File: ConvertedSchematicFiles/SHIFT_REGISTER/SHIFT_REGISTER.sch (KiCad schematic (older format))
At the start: 10 parts, among them U1 7494

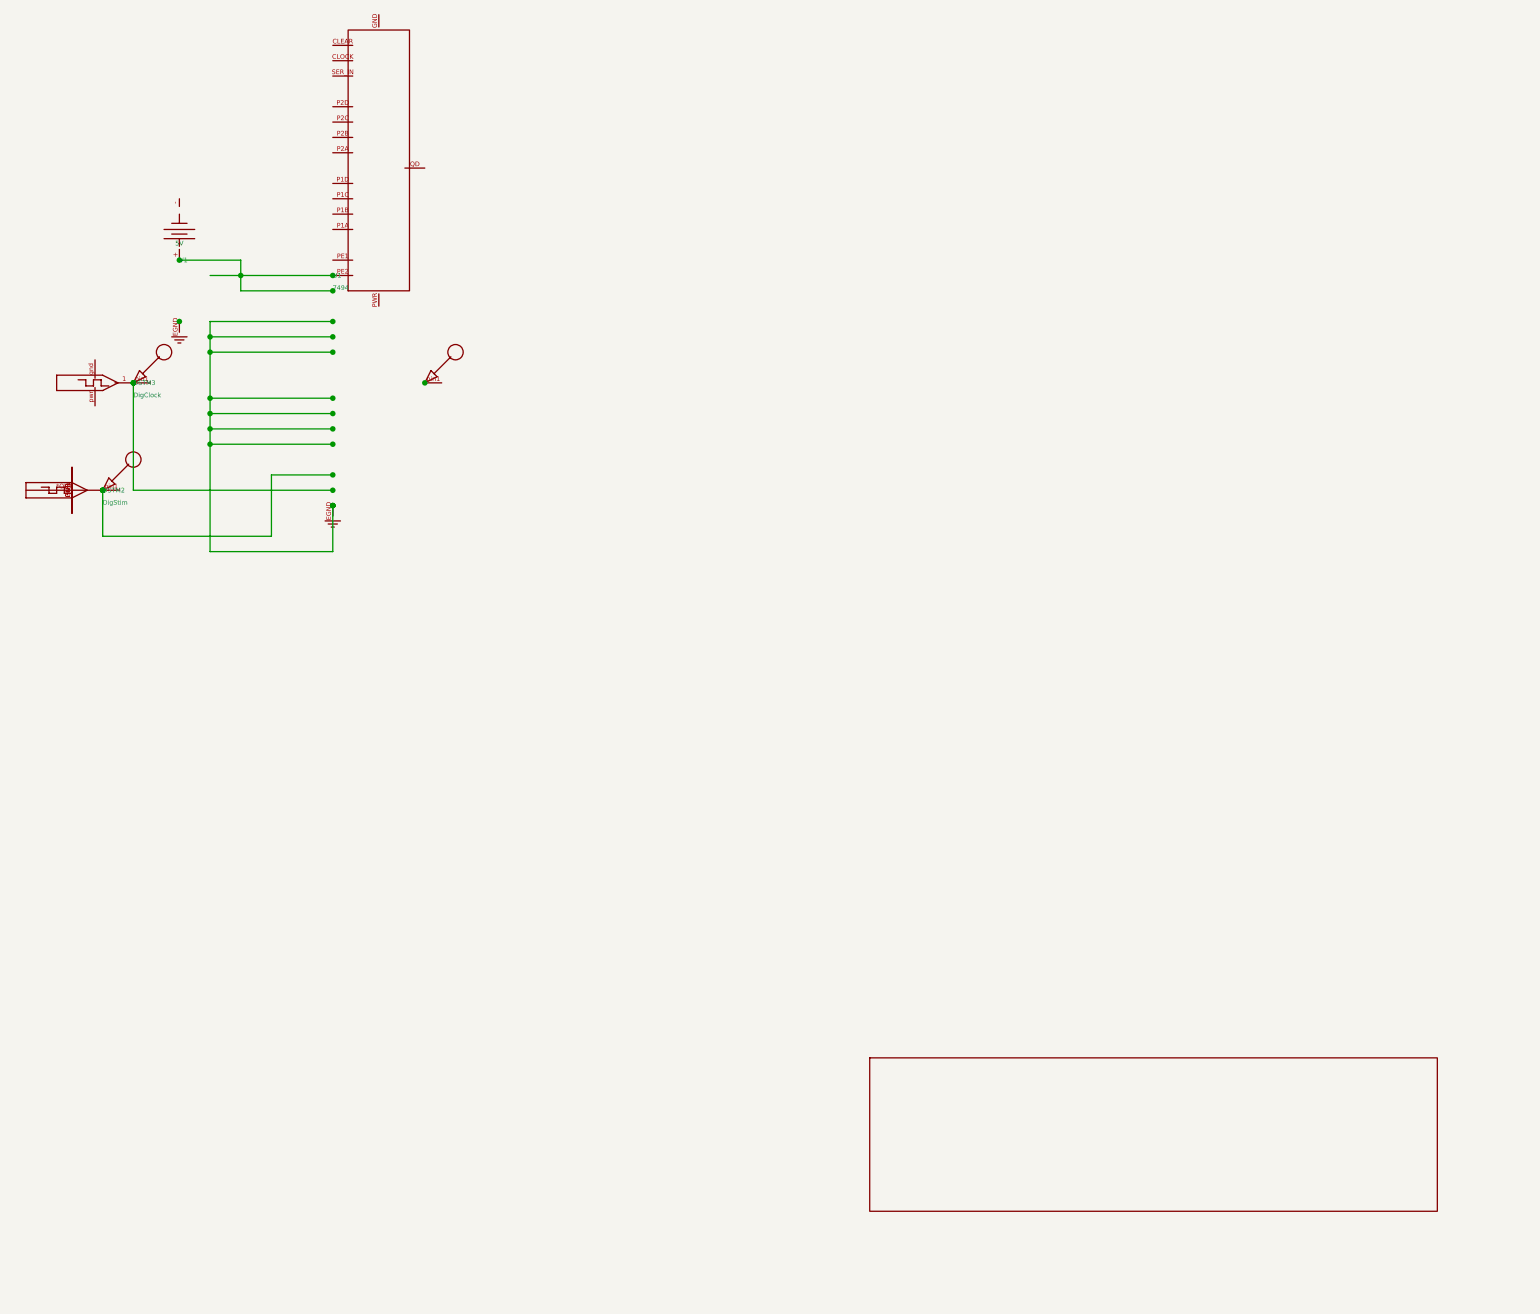
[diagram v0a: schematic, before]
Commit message: Excluded some components. These no longer appear after conversion. When calling shell commands, filenames are in "quotes"
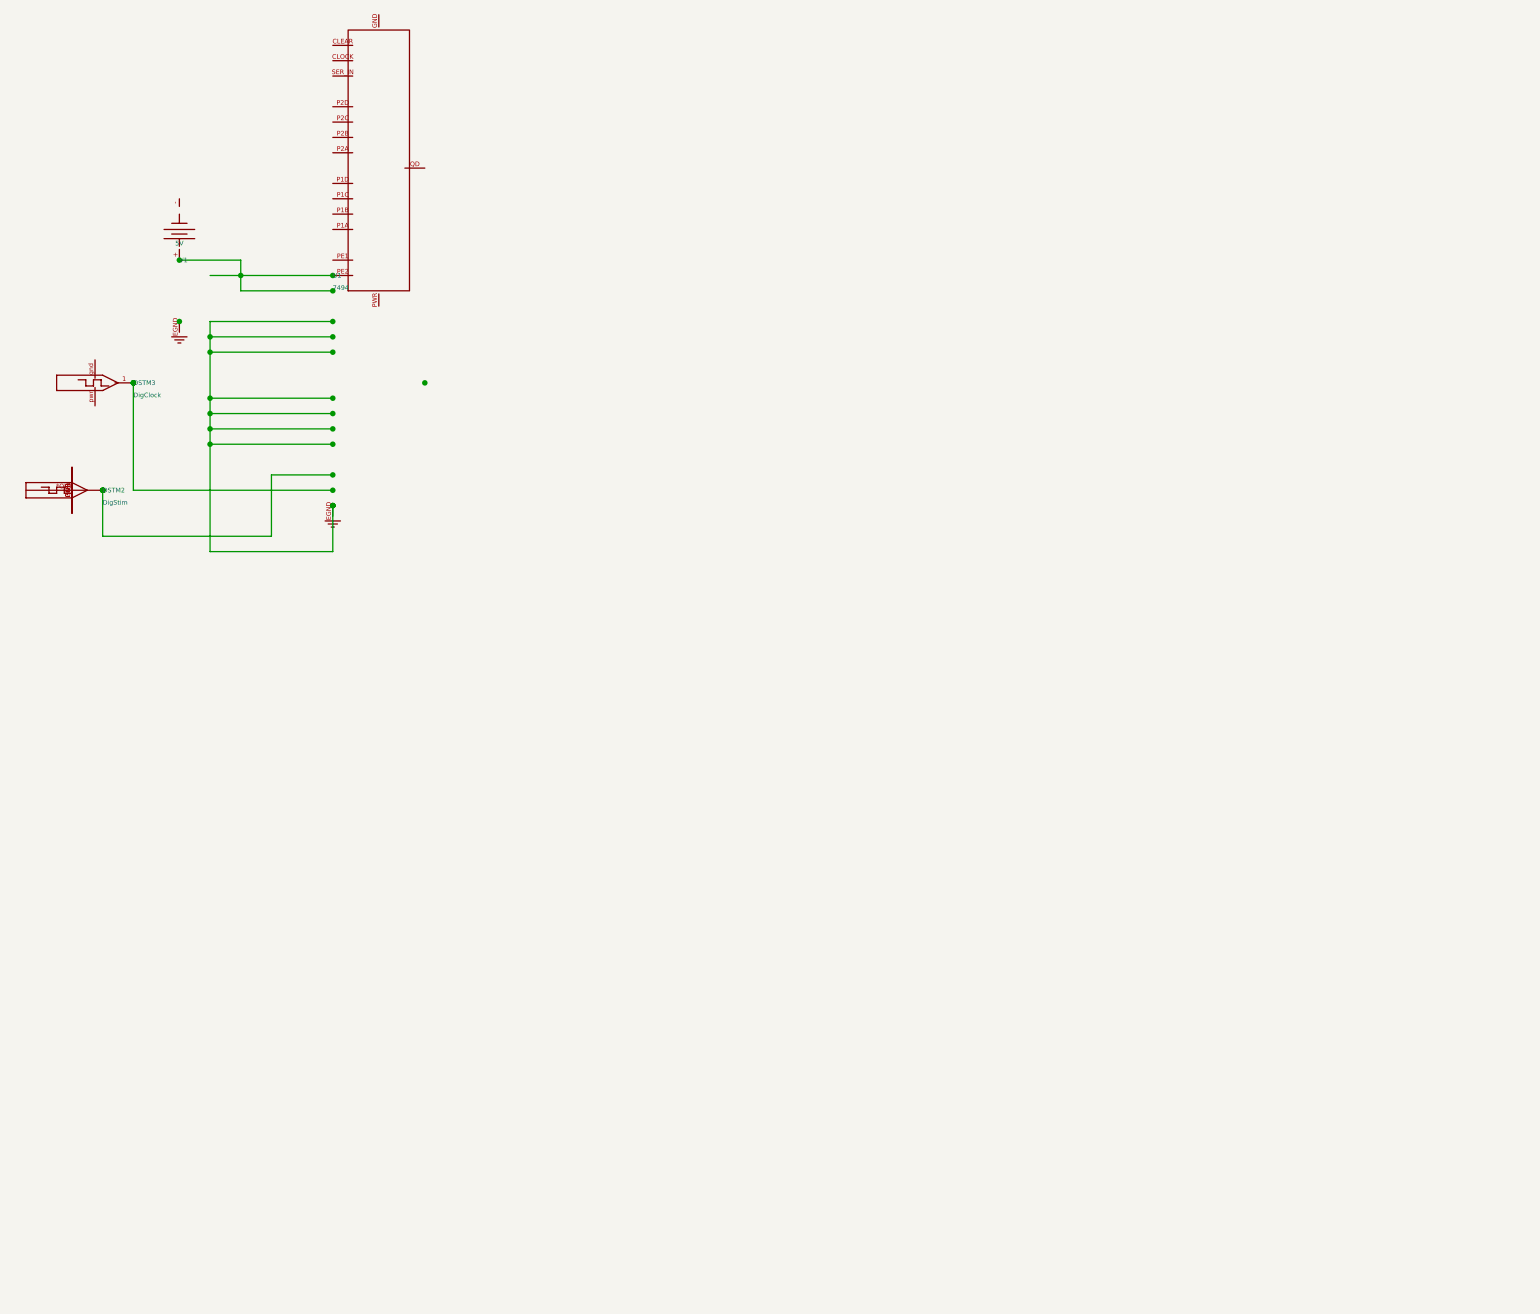
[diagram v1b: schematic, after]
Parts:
- removed nodeMarker (x3): nodeMarker, symbol NODEMARKER_PSPICE
- removed titleblk: titleblk, symbol TITLEBLK_PSPICE
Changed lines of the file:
@@
-	1    0    0    1
-$EndComp
-$Comp
-L TITLEBLK_PSPICE titleblk
-U 1 1 99885386
-P 9700 7200
-F 0 "titleblk" H 19400 14400 30  0001 L CNN
-F 1 "titleblk" H 19400 14480 30  0001 L CNN
-	1    9700 7200
-	1    0    0    1
-$EndComp
-$Comp
-L NODEMARKER_PSPICE nodeMarker
-U 1 1 39760492
-P 3100 1800
-F 0 "nodeMarker" H 6200 3600 30  0001 L CNN
-F 1 "nodeMarker" H 6200 3680 30  0001 L CNN
-	1    3100 1800
-	1    0    0    1
-$EndComp
-$Comp
-L NODEMARKER_PSPICE nodeMarker
-U 1 1 66516649
-P 1000 2500
-F 0 "nodeMarker" H 2000 5000 30  0001 L CNN
-F 1 "nodeMarker" H 2000 5080 30  0001 L CNN
-	1    1000 2500
-	1    0    0    1
-$EndComp
-$Comp
-L NODEMARKER_PSPICE nodeMarker
-U 1 1 29641421
-P 1200 1800
-F 0 "nodeMarker" H 2400 3600 30  0001 L CNN
-F 1 "nodeMarker" H 2400 3680 30  0001 L CNN
-	1    1200 1800
 	1    0    0    1
 $EndComp

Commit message: Ports issue fixed. Now annotation for ports is #PWR? function added "itos"
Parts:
- removed EGND (x2): EGND, symbol EGND_PSPICE
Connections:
- net labels added: EGND
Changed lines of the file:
@@
 $EndDescr
 $Comp
-L EGND_PSPICE EGND
+L EGND_PSPICE #PWR1
 U 1 1 14289383
 P 1500 1400
-F 0 "EGND" H 3000 2800 30  0001 L CNN
+F 0 "#PWR1" H 3000 2800 30  0001 L CNN
 F 1 "EGND" H 3000 2880 30  0001 L CNN
 	1    1500 1400
@@
 $EndComp
 $Comp
-L EGND_PSPICE EGND
+L EGND_PSPICE #PWR2
 U 1 1 46930886
 P 2500 2600
-F 0 "EGND" H 5000 5200 30  0001 L CNN
+F 0 "#PWR2" H 5000 5200 30  0001 L CNN
 F 1 "EGND" H 5000 5280 30  0001 L CNN
 	1    2500 2600

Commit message: Added LICENSE.txt
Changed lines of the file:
@@
 $EndDescr
 $Comp
-L EGND_PSPICE #PWR1
+L GND #PWR1
 U 1 1 14289383
 P 1500 1400
@@
 $EndComp
 $Comp
-L EGND_PSPICE #PWR2
+L GND #PWR2
 U 1 1 46930886
 P 2500 2600

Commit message: Orientation fix. Library components are now inverted, with +ve y axis going up. In Schematic files, +ve y axis is downwards. This is how the KiCad libraries are. As a result of the above fixed, the converted GND is now oriented correctly.
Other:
- moved on the sheet: U1, V1
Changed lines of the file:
@@
 F 1 "EGND" H 3000 2880 30  0001 L CNN
 	1    1500 1400
-	1    0    0    1
+	1    0    0    -1
 $EndComp
 $Comp
@@
 F 1 "EGND" H 5000 5280 30  0001 L CNN
 	1    2500 2600
-	1    0    0    1
+	1    0    0    -1
 $EndComp
 $Comp
@@
 F 1 "DigStim" H 1000 2580 30  0000 L CNN
 	1    1000 2500
-	1    0    0    1
+	1    0    0    -1
 $EndComp
 $Comp
@@
 F 1 "DigClock" H 1200 1880 30  0000 L CNN
 	1    1200 1800
-	1    0    0    1
+	1    0    0    -1
 $EndComp
 $Comp
@@
 F 1 "5V" H 1500 890 30  0000 C CNN
 	1    1500 1000
-	1    0    0    1
+	1    0    0    -1
 $EndComp
 $Comp
@@
 F 1 "7494" H 2500 1180 30  0000 L CNN
 	1    2500 1100
-	1    0    0    1
+	1    0    0    -1
 $EndComp
 Wire Wire Line

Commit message: Removed the use of exec, wrote basename function, made integration with eSim easier.
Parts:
- added nodeMarker (x3): nodeMarker, symbol nodeMarker_PSPICE
- added titleblk: titleblk, symbol titleblk_PSPICE
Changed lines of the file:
@@
-EESchema Schematic File Version 2  date Sunday 05 March 2000 04:20:46 PM IST
+EESchema Schematic File Version 2  date
 LIBS:power
 LIBS:device
@@
 LIBS:contrib
 LIBS:valves
-LIBS:ConvertedSchematicFiles/SHIFT_REGISTER-cache
 EELAYER 25  0
 EELAYER END
@@
 Sheet 1 1
 Title ""
-Date "05 Mar 2000"
+Date ""
 Rev ""
 Comp ""
@@
 	1    0    0    -1
 $EndComp
+$Comp
+L titleblk_PSPICE titleblk
+U 1 1 99885386
+P 9700 7200
+F 0 "titleblk" H 19400 14400 30  0001 L CNN
+F 1 "titleblk" H 19400 14480 30  0001 L CNN
+	1    9700 7200
+	1    0    0    -1
+$EndComp
+$Comp
+L nodeMarker_PSPICE nodeMarker
+U 1 1 39760492
+P 3100 1800
+F 0 "nodeMarker" H 6200 3600 30  0001 L CNN
+F 1 "nodeMarker" H 6200 3680 30  0001 L CNN
+	1    3100 1800
+	1    0    0    -1
+$EndComp
+$Comp
+L nodeMarker_PSPICE nodeMarker
+U 1 1 66516649
+P 1000 2500
+F 0 "nodeMarker" H 2000 5000 30  0001 L CNN
+F 1 "nodeMarker" H 2000 5080 30  0001 L CNN
+	1    1000 2500
+	1    0    0    -1
+$EndComp
+$Comp
+L nodeMarker_PSPICE nodeMarker
+U 1 1 29641421
+P 1200 1800
+F 0 "nodeMarker" H 2400 3600 30  0001 L CNN
+F 1 "nodeMarker" H 2400 3680 30  0001 L CNN
+	1    1200 1800
+	1    0    0    -1
+$EndComp
